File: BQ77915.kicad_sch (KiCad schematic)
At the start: 24 parts, among them U1 BQ7791500PWR

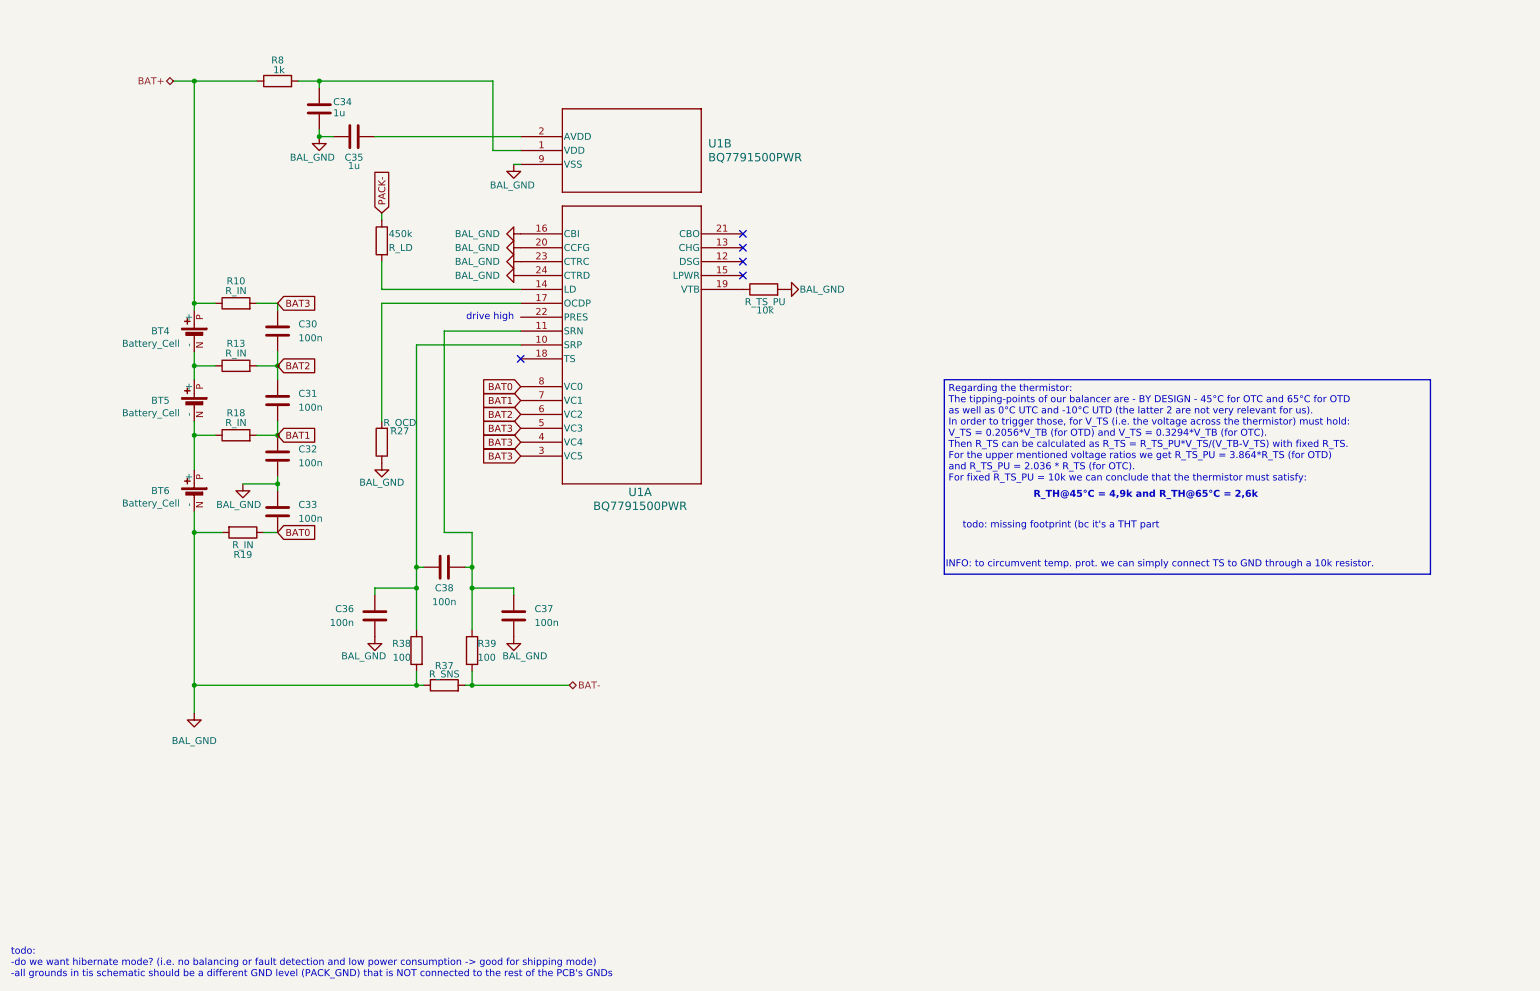
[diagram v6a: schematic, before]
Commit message: finalized new balancer layout (removed R_SNS and implemented the resulting consequences); removed charger shipping mode
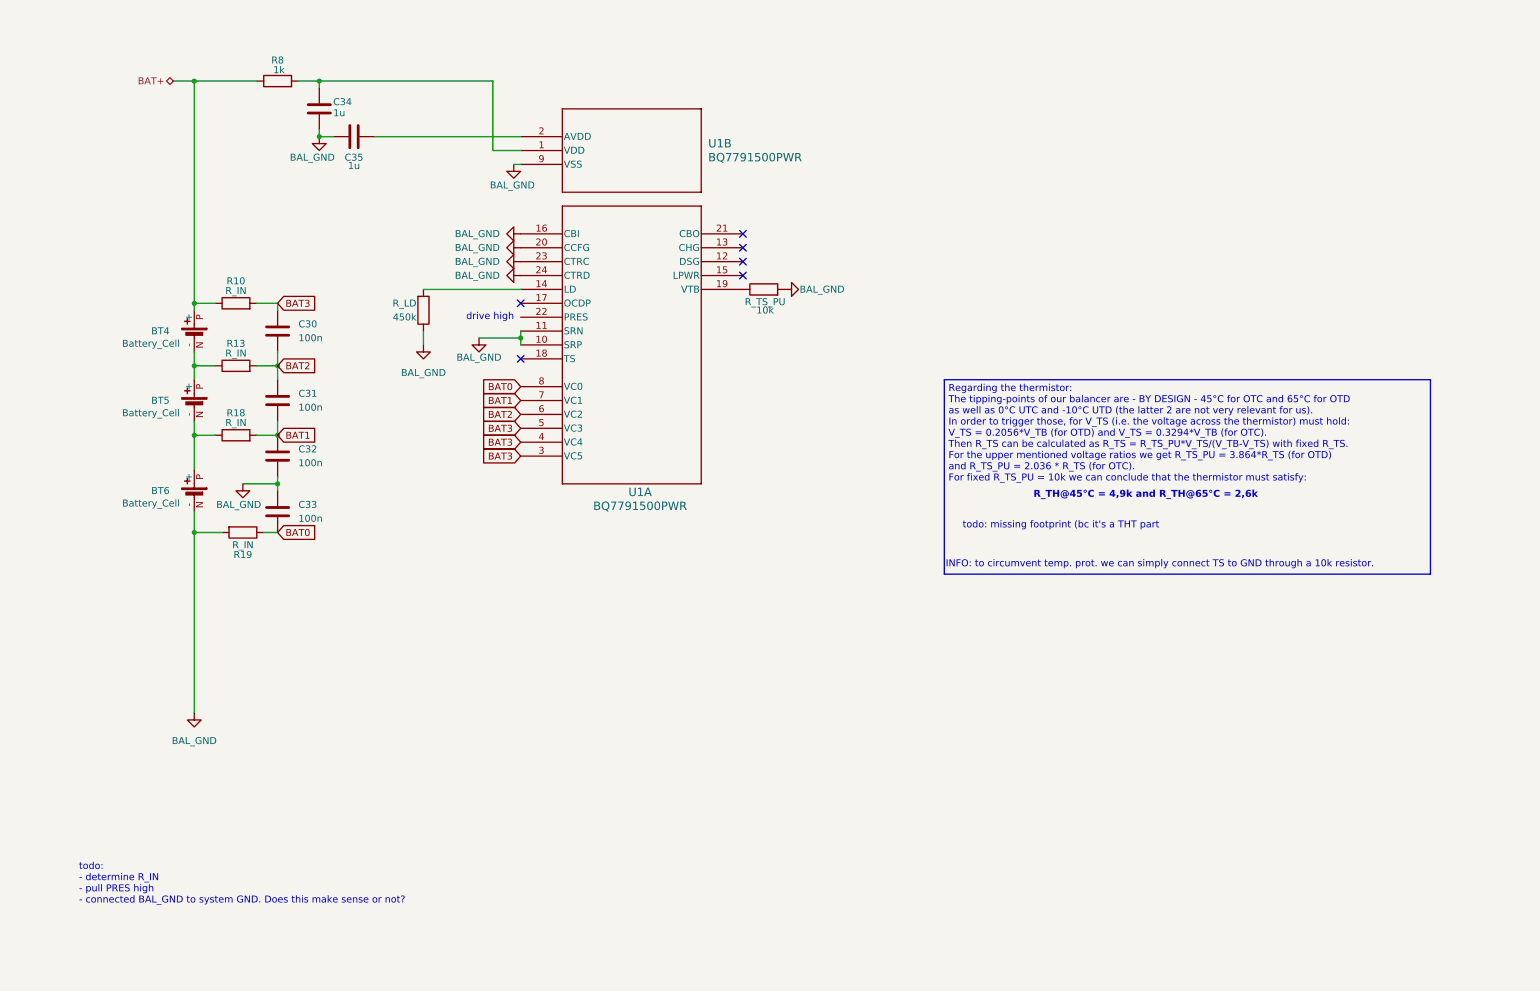
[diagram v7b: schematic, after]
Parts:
- removed C36, C37, C38: 100n, symbol Device:C
- removed R27: R_OCD, symbol Device:R
- removed R37: R_SNS, symbol Device:R
- removed R38, R39: 100, symbol Device:R
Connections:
- net PACK- is gone; now on net BAL_GND: R_LD.1
- net BAL_GND: now also U1.10 (SRP), U1.11 (SRN)
- no-connect marks 5 -> 6
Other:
- note added: "todo: - determine R_IN - pull PRES high - connected BAL_GND to system GND. Does this make sense or not?"
- note removed: "todo: -do we want hibernate mode? (i.e. no balancing or fault detection and low power consumption -> good for shipping mode) -all grounds in tis schematic should be a different GND level (PACK_GND) that is NOT connected to the rest of the PCB's GNDs"
- moved on the sheet: R_LD

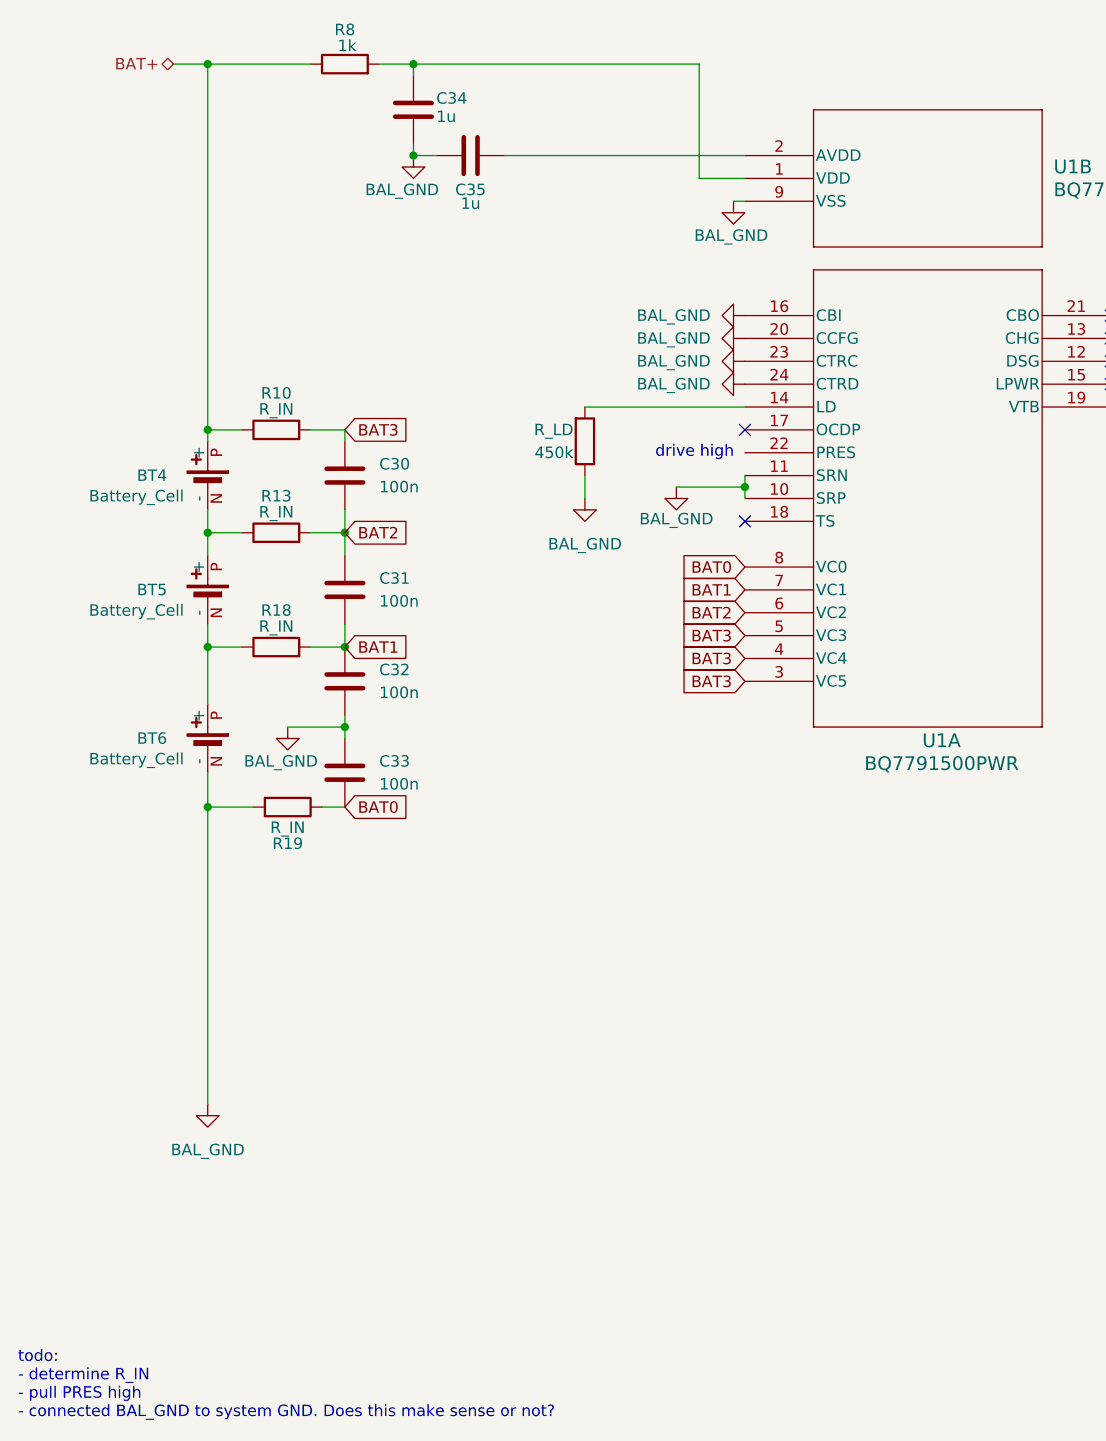
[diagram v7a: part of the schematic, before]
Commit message: changed arming_pin2battery connection
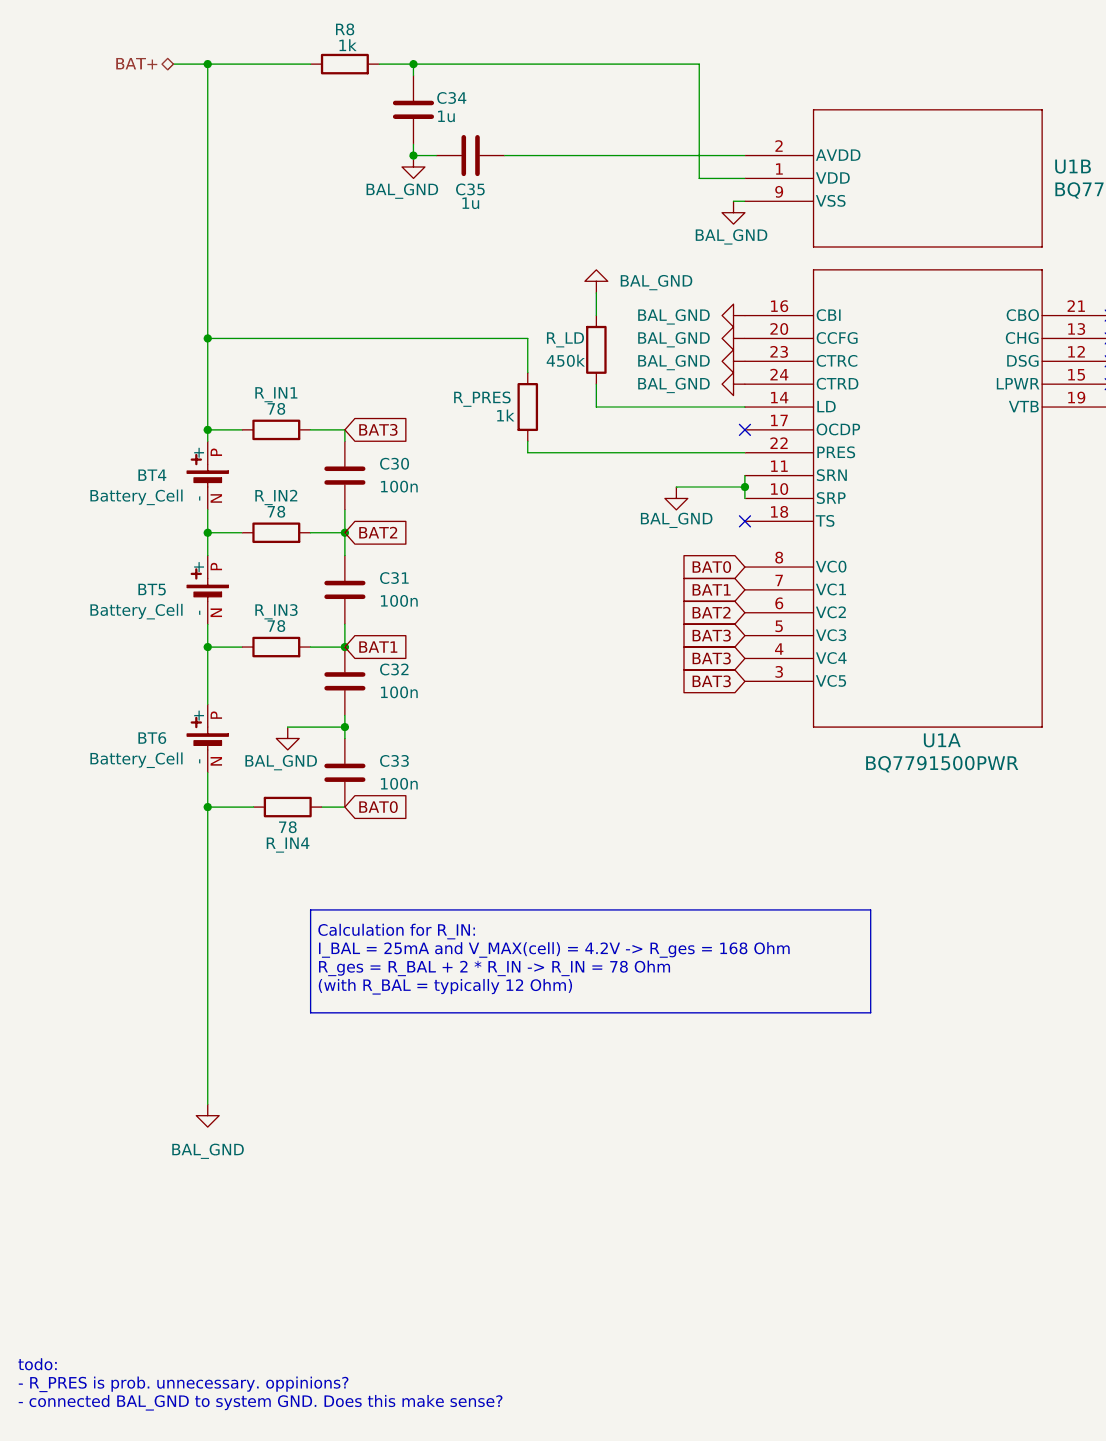
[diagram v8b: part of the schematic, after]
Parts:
- removed R13, R18, R19: R_IN, symbol Device:R
- added R_IN2, R_IN3, R_IN4: 78, symbol Device:R
- added R_PRES: 1k, symbol Device:R
- R_IN1: renamed from R10; value R_IN -> 78
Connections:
- net BAL_GND: now also R_LD.2, R_IN4.2; no longer R_LD.1
- net BAT+: now also R_PRES.1
- net BAT0: now also R_IN4.1
- net BAT1: now also R_IN3.2
- net BAT2: now also R_IN2.2
- net at U1.14 (LD): now also R_LD.1; no longer R_LD.2
- net at BT5.N (-), BT6.P (+): now also R_IN3.1
- net at BT4.N (-), BT5.P (+): now also R_IN2.1
- net at U1.22 (PRES): now also R_PRES.2
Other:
- note added: "Calculation for R_IN: I_BAL = 25mA and V_MAX(cell) = 4.2V -> R_ges = 168 Ohm R_ges = R_BAL + 2 * R_IN -> R_IN = 78 Ohm (with R_BAL = typically 12 Ohm)"
- note added: "todo: - R_PRES is prob. unnecessary. oppinions? - connected BAL_GND to system GND. Does this make sense?"
- note removed: "drive high"
- note removed: "todo: - determine R_IN - pull PRES high - connected BAL_GND to system GND. Does this make sense or not?"
- moved on the sheet: R_LD
